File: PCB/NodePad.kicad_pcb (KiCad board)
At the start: 4 copper layers, 100 x 100 mm, 0 parts

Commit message: auto-commit for 1e42cf4f-3af1-430f-b4bd-a55f7dad9cb4
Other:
- board text added: "CERN-OHL-P v2 - Made with love"
- board text added: "Samrath Sami Singh"
- board text added: "by Samrath Sami Singh"
- board text added: "github.com/Sami9889/NodePad"
- board text removed: "Sami9889 - CERN-OHL-P v2"
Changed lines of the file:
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@@
 	(gr_text "NodePad" (at 50 20 0) (layer "F.SilkS")
 		(effects (font (size 3 3) (thickness 0.5) (bold yes)) (justify bottom)))
-	(gr_text "Radxa CM5 carrier - rev 0.1" (at 50 25 0) (layer "F.SilkS")
-		(effects (font (size 1.2 1.2) (thickness 0.2)) (justify bottom)))
-	(gr_text "Sami9889 - CERN-OHL-P v2" (at 50 92 0) (layer "F.SilkS")
+	(gr_text "by Samrath Sami Singh" (at 50 24 0) (layer "F.SilkS")
+		(effects (font (size 1.5 1.5) (thickness 0.25) (italic yes)) (justify bottom)))
+	(gr_text "Radxa CM5 carrier - rev 0.1" (at 50 28 0) (layer "F.SilkS")
+		(effects (font (size 1 1) (thickness 0.15)) (justify bottom)))
+	(gr_text "github.com/Sami9889/NodePad" (at 50 92 0) (layer "F.SilkS")
 		(effects (font (size 1 1) (thickness 0.15)) (justify top)))
+	(gr_text "Samrath Sami Singh" (at 50 8 0) (layer "B.SilkS")
+		(effects (font (size 2 2) (thickness 0.3) (bold yes)) (justify bottom mirror)))
+	(gr_text "CERN-OHL-P v2  -  Made with love" (at 50 12 0) (layer "B.SilkS")
+		(effects (font (size 1 1) (thickness 0.15) (italic yes)) (justify bottom mirror)))
 	(gr_text "CM5 SoM zone" (at 50 55 0) (layer "F.Fab")
 		(effects (font (size 2 2) (thickness 0.3))))

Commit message: Auto-generated changes
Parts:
- added BT1: CR2032, BatteryHolder_Keystone_3002_1x2032, F.Cu at (10.0, 45.0)
- added C1: 1uF, C_0402_1005Metric, F.Cu at (15.5, 45.0)
- added C10: 22uF/25V, C_0805_2012Metric, F.Cu at (21.0, 45.0)
- added C11: 22uF/25V, C_0805_2012Metric, F.Cu at (26.5, 45.0)
- added C12: 10uF/16V, C_0402_1005Metric, F.Cu at (32.0, 45.0)
- added C13: 100nF, C_0402_1005Metric, F.Cu at (37.5, 45.0)
- added C15: 1uF, C_0402_1005Metric, F.Cu at (43.0, 45.0)
- added C16: 1uF, C_0402_1005Metric, F.Cu at (48.5, 45.0)
- added C2: 1uF, C_0402_1005Metric, F.Cu at (54.0, 45.0)
- added C3: 22uF/25V, C_0805_2012Metric, F.Cu at (59.5, 45.0)
- added C4: 100nF, C_0402_1005Metric, F.Cu at (65.0, 45.0)
- added C5: 2.2nF, C_0402_1005Metric, F.Cu at (70.5, 45.0)
- added C6: 100pF, C_0402_1005Metric, F.Cu at (76.0, 45.0)
- added C_AVDD_BULK_1: 10uF, C_0805_2012Metric, F.Cu at (81.5, 45.0)
- added C_AVDD_BULK_2: 10uF, C_0805_2012Metric, F.Cu at (87.0, 45.0)
- added C_AVDD_BULK_3: 10uF, C_0805_2012Metric, F.Cu at (92.5, 45.0)
- added C_AVDD_BULK_4: 10uF, C_0805_2012Metric, F.Cu at (10.0, 50.5)
- added C_AVDD_HF_1: 100nF, C_0402_1005Metric, F.Cu at (15.5, 50.5)
- added C_AVDD_HF_2: 100nF, C_0402_1005Metric, F.Cu at (21.0, 50.5)
- added C_AVDD_HF_3: 100nF, C_0402_1005Metric, F.Cu at (26.5, 50.5)
- added C_AVDD_HF_4: 100nF, C_0402_1005Metric, F.Cu at (32.0, 50.5)
- added C_BAT_1: 100nF, C_0402_1005Metric, F.Cu at (37.5, 50.5)
- added C_BLK_3V3_AUX_01: 10uF, C_0805_2012Metric, F.Cu at (43.0, 50.5)
- added C_BLK_3V3_AUX_02: 10uF, C_0805_2012Metric, F.Cu at (48.5, 50.5)
- added C_BLK_3V3_AUX_03: 10uF, C_0805_2012Metric, F.Cu at (54.0, 50.5)
- added C_BLK_5V_01: 10uF, C_0805_2012Metric, F.Cu at (59.5, 50.5)
- added C_BLK_5V_02: 10uF, C_0805_2012Metric, F.Cu at (65.0, 50.5)
- added C_BLK_5V_03: 10uF, C_0805_2012Metric, F.Cu at (70.5, 50.5)
- added C_BLK_5V_04: 10uF, C_0805_2012Metric, F.Cu at (76.0, 50.5)
- added C_BS_J3: 1nF/2kV, C_1210_3225Metric, F.Cu at (81.5, 50.5)
- added C_BS_J4: 1nF/2kV, C_1210_3225Metric, F.Cu at (87.0, 50.5)
- added C_CM5_BULK_1: 10uF, C_0603_1608Metric, F.Cu at (92.5, 50.5)
- added C_CM5_BULK_2: 10uF, C_0603_1608Metric, F.Cu at (10.0, 56.0)
- added C_CM5_BULK_3: 10uF, C_0603_1608Metric, F.Cu at (15.5, 56.0)
- added C_CM5_BULK_4: 10uF, C_0603_1608Metric, F.Cu at (21.0, 56.0)
- added C_CM5_BULK_5: 10uF, C_0603_1608Metric, F.Cu at (26.5, 56.0)
- added C_CM5_BULK_6: 10uF, C_0603_1608Metric, F.Cu at (32.0, 56.0)
- added C_CM5_HF_1: 100nF, C_0402_1005Metric, F.Cu at (37.5, 56.0)
- added C_CM5_HF_10: 100nF, C_0402_1005Metric, F.Cu at (43.0, 56.0)
- added C_CM5_HF_2: 100nF, C_0402_1005Metric, F.Cu at (48.5, 56.0)
- added C_CM5_HF_3: 100nF, C_0402_1005Metric, F.Cu at (54.0, 56.0)
- added C_CM5_HF_4: 100nF, C_0402_1005Metric, F.Cu at (59.5, 56.0)
- added C_CM5_HF_5: 100nF, C_0402_1005Metric, F.Cu at (65.0, 56.0)
- added C_CM5_HF_6: 100nF, C_0402_1005Metric, F.Cu at (70.5, 56.0)
- added C_CM5_HF_7: 100nF, C_0402_1005Metric, F.Cu at (76.0, 56.0)
- added C_CM5_HF_8: 100nF, C_0402_1005Metric, F.Cu at (81.5, 56.0)
- added C_CM5_HF_9: 100nF, C_0402_1005Metric, F.Cu at (87.0, 56.0)
- added C_DEC_3V3_AUX_01: 100nF, C_0402_1005Metric, F.Cu at (92.5, 56.0)
- added C_DEC_3V3_AUX_02: 100nF, C_0402_1005Metric, F.Cu at (10.0, 61.5)
- added C_DEC_3V3_AUX_03: 100nF, C_0402_1005Metric, F.Cu at (15.5, 61.5)
- added C_DEC_3V3_AUX_04: 100nF, C_0402_1005Metric, F.Cu at (21.0, 61.5)
- added C_DEC_3V3_AUX_05: 100nF, C_0402_1005Metric, F.Cu at (26.5, 61.5)
- added C_DEC_3V3_AUX_06: 100nF, C_0402_1005Metric, F.Cu at (32.0, 61.5)
- added C_DEC_3V3_AUX_07: 100nF, C_0402_1005Metric, F.Cu at (37.5, 61.5)
- added C_DEC_3V3_AUX_08: 100nF, C_0402_1005Metric, F.Cu at (43.0, 61.5)
- added C_DEC_3V3_AUX_09: 100nF, C_0402_1005Metric, F.Cu at (48.5, 61.5)
- added C_DEC_3V3_AUX_10: 100nF, C_0402_1005Metric, F.Cu at (54.0, 61.5)
- added C_DEC_5V_01: 100nF, C_0402_1005Metric, F.Cu at (59.5, 61.5)
- added C_DEC_5V_02: 100nF, C_0402_1005Metric, F.Cu at (65.0, 61.5)
- added C_DEC_5V_03: 100nF, C_0402_1005Metric, F.Cu at (70.5, 61.5)
- added C_DEC_5V_04: 100nF, C_0402_1005Metric, F.Cu at (76.0, 61.5)
- added C_DEC_5V_05: 100nF, C_0402_1005Metric, F.Cu at (81.5, 61.5)
- added C_DEC_5V_06: 100nF, C_0402_1005Metric, F.Cu at (87.0, 61.5)
- added C_DEC_5V_07: 100nF, C_0402_1005Metric, F.Cu at (92.5, 61.5)
- added C_DEC_5V_08: 100nF, C_0402_1005Metric, F.Cu at (10.0, 67.0)
- added C_DEC_5V_09: 100nF, C_0402_1005Metric, F.Cu at (15.5, 67.0)
- added C_DEC_5V_10: 100nF, C_0402_1005Metric, F.Cu at (21.0, 67.0)
- added C_DEC_5V_11: 100nF, C_0402_1005Metric, F.Cu at (26.5, 67.0)
- added C_DEC_5V_12: 100nF, C_0402_1005Metric, F.Cu at (32.0, 67.0)
- added C_EMI: 1nF/2kV, C_1210_3225Metric, F.Cu at (37.5, 67.0)
- added C_HUB_1: 100nF, C_0402_1005Metric, F.Cu at (43.0, 67.0)
- added C_HUB_2: 100nF, C_0402_1005Metric, F.Cu at (48.5, 67.0)
- added C_HUB_3: 100nF, C_0402_1005Metric, F.Cu at (54.0, 67.0)
- added C_HUB_4: 100nF, C_0402_1005Metric, F.Cu at (59.5, 67.0)
- added C_HUB_5: 100nF, C_0402_1005Metric, F.Cu at (65.0, 67.0)
- added C_HUB_6: 100nF, C_0402_1005Metric, F.Cu at (70.5, 67.0)
- added C_HUB_7: 100nF, C_0402_1005Metric, F.Cu at (76.0, 67.0)
- added C_HUB_8: 100nF, C_0402_1005Metric, F.Cu at (81.5, 67.0)
- added C_HUB_BULK: 10uF, C_0603_1608Metric, F.Cu at (87.0, 67.0)
- added C_HUB_LDO: 4.7uF, C_0603_1608Metric, F.Cu at (92.5, 67.0)
- added C_M2E_1: 100nF, C_0402_1005Metric, F.Cu at (10.0, 72.5)
- added C_M2E_2: 100nF, C_0402_1005Metric, F.Cu at (15.5, 72.5)
- added C_M2E_3: 100nF, C_0402_1005Metric, F.Cu at (21.0, 72.5)
- added C_M2E_BULK: 10uF, C_0603_1608Metric, F.Cu at (26.5, 72.5)
- added C_M2M_1: 100nF, C_0402_1005Metric, F.Cu at (32.0, 72.5)
- added C_M2M_2: 100nF, C_0402_1005Metric, F.Cu at (37.5, 72.5)
- added C_M2M_3: 100nF, C_0402_1005Metric, F.Cu at (43.0, 72.5)
- added C_M2M_4: 100nF, C_0402_1005Metric, F.Cu at (48.5, 72.5)
- added C_M2M_BULK: 22uF/6.3V, C_0805_2012Metric, F.Cu at (54.0, 72.5)
- added C_POE_BULK: 22uF/100V DNP, C_1210_3225Metric, F.Cu at (59.5, 72.5)
- added C_POE_HF: 100nF/100V DNP, C_1206_3216Metric, F.Cu at (65.0, 72.5)
- added C_POE_SEC: 47uF/25V DNP, C_1210_3225Metric, F.Cu at (70.5, 72.5)
- added C_PWR_EN_DLY: 470nF, C_0402_1005Metric, F.Cu at (76.0, 72.5)
- added C_RESET_DB: 100nF, C_0402_1005Metric, F.Cu at (81.5, 72.5)
- added C_RTC_1: 100nF, C_0402_1005Metric, F.Cu at (87.0, 72.5)
- added C_RTC_2: 1uF, C_0402_1005Metric, F.Cu at (92.5, 72.5)
- added C_RTL_1: 100nF, C_0402_1005Metric, F.Cu at (10.0, 78.0)
- added C_RTL_2: 100nF, C_0402_1005Metric, F.Cu at (15.5, 78.0)
- added C_RTL_3: 100nF, C_0402_1005Metric, F.Cu at (21.0, 78.0)
- added C_RTL_4: 100nF, C_0402_1005Metric, F.Cu at (26.5, 78.0)
- added C_RTL_5: 100nF, C_0402_1005Metric, F.Cu at (32.0, 78.0)
- added C_RTL_6: 100nF, C_0402_1005Metric, F.Cu at (37.5, 78.0)
- added C_RTL_BULK: 10uF, C_0603_1608Metric, F.Cu at (43.0, 78.0)
- added C_VB_J10: 150uF/6.3V, C_1206_3216Metric, F.Cu at (48.5, 78.0)
- added C_VB_J11: 150uF/6.3V, C_1206_3216Metric, F.Cu at (54.0, 78.0)
- added C_VB_J8: 150uF/6.3V, C_1206_3216Metric, F.Cu at (59.5, 78.0)
- added C_VB_J9: 150uF/6.3V, C_1206_3216Metric, F.Cu at (65.0, 78.0)
- added C_VIN_BULK: 47uF/25V, CP_Elec_5x5.4, F.Cu at (70.5, 78.0)
- added C_VIN_HF: 100nF, C_0402_1005Metric, F.Cu at (76.0, 78.0)
- added D1: Green, LED_0603_1608Metric, F.Cu at (81.5, 78.0)
- added D2: Blue, LED_0603_1608Metric, F.Cu at (87.0, 78.0)
- added D3: Yellow, LED_0603_1608Metric, F.Cu at (92.5, 78.0)
- added D4: Yellow, LED_0603_1608Metric, F.Cu at (10.0, 83.5)
- added D5: Red, LED_0603_1608Metric, F.Cu at (15.5, 83.5)
- added D6: SMBJ12A, D_SMB, F.Cu at (21.0, 83.5)
- added D_BAT: BAT54, D_SOD-323, F.Cu at (26.5, 83.5)
- added D_HDMI_CTL_1: ESD5Z5.0, D_SOD-523, F.Cu at (32.0, 83.5)
- added D_HDMI_CTL_2: ESD5Z5.0, D_SOD-523, F.Cu at (37.5, 83.5)
- added D_POE_1: HD01-T DNP, D_SMB, F.Cu at (43.0, 83.5)
- added D_POE_2: HD01-T DNP, D_SMB, F.Cu at (48.5, 83.5)
- added D_POE_3: HD01-T DNP, D_SMB, F.Cu at (54.0, 83.5)
- added D_POE_4: HD01-T DNP, D_SMB, F.Cu at (59.5, 83.5)
- added D_POE_OR: SS36 DNP, D_SMB, F.Cu at (65.0, 83.5)
- added D_POE_SEC: SS36 DNP, D_SMB, F.Cu at (70.5, 83.5)
- added D_POE_TVS: SMBJ58A DNP, D_SMB, F.Cu at (76.0, 83.5)
- added D_TVS_J10: SMBJ5.0A, D_SMB, F.Cu at (81.5, 83.5)
- added D_TVS_J11: SMBJ5.0A, D_SMB, F.Cu at (87.0, 83.5)
- added D_TVS_J8: SMBJ5.0A, D_SMB, F.Cu at (92.5, 83.5)
- added D_TVS_J9: SMBJ5.0A, D_SMB, F.Cu at (10.0, 89.0)
- added FB_AVDD_1: 600R@100MHz, L_0603_1608Metric, F.Cu at (15.5, 89.0)
- added FB_AVDD_2: 600R@100MHz, L_0603_1608Metric, F.Cu at (21.0, 89.0)
- added FB_AVDD_3: 600R@100MHz, L_0603_1608Metric, F.Cu at (26.5, 89.0)
- added FB_AVDD_4: 600R@100MHz, L_0603_1608Metric, F.Cu at (32.0, 89.0)
- added FB_HDMI_5V: 600R@100MHz, L_0603_1608Metric, F.Cu at (37.5, 89.0)
- added J1: CM5-J1, Hirose_BM24_BM24-40DS-2-0.35V_2x20_P0.35mm_PowerPin2_Vertical, F.Cu at (43.0, 89.0)
- added J10: USB3-A, USB3_A_Molex_48393-001, F.Cu at (48.5, 89.0)
- added J11: USB3-A, USB3_A_Molex_48393-001, F.Cu at (54.0, 89.0)
- added J12: HDMI, HDMI_A_Molex_208658-1001_Horizontal, F.Cu at (59.5, 89.0)
- added J13: GPIO40, PinHeader_2x20_P2.54mm_Vertical, F.Cu at (65.0, 89.0)
- added J15: Fan, PinHeader_1x04_P2.54mm_Vertical, F.Cu at (70.5, 89.0)
- added J2: CM5-J2, Hirose_BM24_BM24-40DS-2-0.35V_2x20_P0.35mm_PowerPin2_Vertical, F.Cu at (76.0, 89.0)
- added J3: RJ45, RJ45_Amphenol_RJHSE538X-02, F.Cu at (81.5, 89.0)
- added J4: RJ45, RJ45_Amphenol_RJHSE538X-02, F.Cu at (87.0, 89.0)
- added J5: M.2 M-key 2280, PinHeader_2x38_P1.27mm_Vertical_SMD, F.Cu at (92.5, 89.0)
- added J6: M.2 E-key 2230, PinHeader_2x38_P1.27mm_Vertical_SMD, F.Cu at (10.0, 94.5)
- added J7: USB-C, USB_C_Receptacle_HRO_TYPE-C-31-M-12, F.Cu at (15.5, 94.5)
- added J8: USB3-A, USB3_A_Molex_48393-001, F.Cu at (21.0, 94.5)
- added J9: USB3-A, USB3_A_Molex_48393-001, F.Cu at (26.5, 94.5)
- added L1: 4.7uH/3A, L_Bourns_SRR1208_12.7x12.7mm, F.Cu at (32.0, 94.5)
- added MH1: M2.5 heatsink, MountingHole_2.7mm_M2.5, F.Cu at (37.5, 94.5)
- added MH2: M2.5 heatsink, MountingHole_2.7mm_M2.5, F.Cu at (43.0, 94.5)
- added MH3: M2.5 heatsink, MountingHole_2.7mm_M2.5, F.Cu at (48.5, 94.5)
- added MH4: M2.5 heatsink, MountingHole_2.7mm_M2.5, F.Cu at (54.0, 94.5)
- added Q_DDC_1: BSS138, SOT-23, F.Cu at (59.5, 94.5)
- added Q_DDC_2: BSS138, SOT-23, F.Cu at (65.0, 94.5)
- added R1: 10k, R_0402_1005Metric, F.Cu at (70.5, 94.5)
- added R2: 10k, R_0402_1005Metric, F.Cu at (76.0, 94.5)
- added R3: 0, R_0402_1005Metric, F.Cu at (81.5, 94.5)
- added R4: 100k, R_0402_1005Metric, F.Cu at (87.0, 94.5)
- added R5: 52.3k, R_0402_1005Metric, F.Cu at (92.5, 94.5)
- added R6: 10k, R_0402_1005Metric, F.Cu at (10.0, 100.0)
- added R7: 10k, R_0402_1005Metric, F.Cu at (15.5, 100.0)
- added R_BOOT0_PU: 10k, R_0402_1005Metric, F.Cu at (21.0, 100.0)
- added R_BOOT1_PU: 10k, R_0402_1005Metric, F.Cu at (26.5, 100.0)
- added R_BOOT2_PU: 10k, R_0402_1005Metric, F.Cu at (32.0, 100.0)
- added R_BS_J3_1: 75, R_0402_1005Metric, F.Cu at (37.5, 100.0)
- added R_BS_J3_2: 75, R_0402_1005Metric, F.Cu at (43.0, 100.0)
- added R_BS_J3_3: 75, R_0402_1005Metric, F.Cu at (48.5, 100.0)
- added R_BS_J3_4: 75, R_0402_1005Metric, F.Cu at (54.0, 100.0)
- added R_BS_J3_5: 75, R_0402_1005Metric, F.Cu at (59.5, 100.0)
- added R_BS_J3_6: 75, R_0402_1005Metric, F.Cu at (65.0, 100.0)
- added R_BS_J3_7: 75, R_0402_1005Metric, F.Cu at (70.5, 100.0)
- added R_BS_J3_8: 75, R_0402_1005Metric, F.Cu at (76.0, 100.0)
- added R_BS_J4_1: 75, R_0402_1005Metric, F.Cu at (81.5, 100.0)
- added R_BS_J4_2: 75, R_0402_1005Metric, F.Cu at (87.0, 100.0)
- added R_BS_J4_3: 75, R_0402_1005Metric, F.Cu at (92.5, 100.0)
- added R_BS_J4_4: 75, R_0402_1005Metric, F.Cu at (10.0, 105.5)
- added R_BS_J4_5: 75, R_0402_1005Metric, F.Cu at (15.5, 105.5)
- added R_BS_J4_6: 75, R_0402_1005Metric, F.Cu at (21.0, 105.5)
- added R_BS_J4_7: 75, R_0402_1005Metric, F.Cu at (26.5, 105.5)
- added R_BS_J4_8: 75, R_0402_1005Metric, F.Cu at (32.0, 105.5)
- added R_D1: 1k, R_0402_1005Metric, F.Cu at (37.5, 105.5)
- added R_D2: 1k, R_0402_1005Metric, F.Cu at (43.0, 105.5)
- added R_D3: 1k, R_0402_1005Metric, F.Cu at (48.5, 105.5)
- added R_D4: 1k, R_0402_1005Metric, F.Cu at (54.0, 105.5)
- added R_D5: 1k, R_0402_1005Metric, F.Cu at (59.5, 105.5)
- added R_DDC_G_1: 10k, R_0402_1005Metric, F.Cu at (65.0, 105.5)
- added R_DDC_G_2: 10k, R_0402_1005Metric, F.Cu at (70.5, 105.5)
- added R_DDC_HI_1: 10k, R_0402_1005Metric, F.Cu at (76.0, 105.5)
- added R_DDC_HI_2: 10k, R_0402_1005Metric, F.Cu at (81.5, 105.5)
- added R_DDC_LO_1: 10k, R_0402_1005Metric, F.Cu at (87.0, 105.5)
- added R_DDC_LO_2: 10k, R_0402_1005Metric, F.Cu at (92.5, 105.5)
- added R_DDC_SCL: 2.2k, R_0402_1005Metric, F.Cu at (10.0, 111.0)
- added R_DDC_SCL_SER: 100, R_0402_1005Metric, F.Cu at (15.5, 111.0)
- added R_DDC_SDA: 2.2k, R_0402_1005Metric, F.Cu at (21.0, 111.0)
- added R_DDC_SDA_SER: 100, R_0402_1005Metric, F.Cu at (26.5, 111.0)
- added R_E_OPT_1: 0/DNP, R_0402_1005Metric, F.Cu at (32.0, 111.0)
- added R_E_OPT_2: 0/DNP, R_0402_1005Metric, F.Cu at (37.5, 111.0)
- added R_E_OPT_3: 0/DNP, R_0402_1005Metric, F.Cu at (43.0, 111.0)
- added R_E_OPT_4: 0/DNP, R_0402_1005Metric, F.Cu at (48.5, 111.0)
- added R_HUB_BP: 10k, R_0402_1005Metric, F.Cu at (54.0, 111.0)
- added R_HUB_RST: 10k, R_0402_1005Metric, F.Cu at (59.5, 111.0)
- added R_I2C1_SCL_PU: 4.7k, R_0402_1005Metric, F.Cu at (65.0, 111.0)
- added R_I2C1_SDA_PU: 4.7k, R_0402_1005Metric, F.Cu at (70.5, 111.0)
- added R_ILIM_J10: 30k, R_0402_1005Metric, F.Cu at (76.0, 111.0)
- added R_ILIM_J11: 30k, R_0402_1005Metric, F.Cu at (81.5, 111.0)
- added R_ILIM_J8: 30k, R_0402_1005Metric, F.Cu at (87.0, 111.0)
- added R_ILIM_J9: 30k, R_0402_1005Metric, F.Cu at (92.5, 111.0)
- added R_INT_PU: 10k, R_0402_1005Metric, F.Cu at (10.0, 116.5)
- added R_M2M_PERST: 10k, R_0402_1005Metric, F.Cu at (15.5, 116.5)
- added R_MASKROM_PU: 10k, R_0402_1005Metric, F.Cu at (21.0, 116.5)
- added R_NVME_ACT_PU: 10k, R_0402_1005Metric, F.Cu at (26.5, 116.5)
- added R_PCIE0_TERM_N: 49.9 DNP, R_0402_1005Metric, F.Cu at (32.0, 116.5)
- added R_PCIE0_TERM_P: 49.9 DNP, R_0402_1005Metric, F.Cu at (37.5, 116.5)
- added R_POE_CLASS: 12.5 DNP, R_0402_1005Metric, F.Cu at (43.0, 116.5)
- added R_POE_SIG: 25k DNP, R_0402_1005Metric, F.Cu at (48.5, 116.5)
- added R_PU_PCIE0_CLKREQ: 10k, R_0402_1005Metric, F.Cu at (54.0, 116.5)
- added R_PU_PCIE0_PERST: 10k, R_0402_1005Metric, F.Cu at (59.5, 116.5)
- added R_PU_PCIE1_CLKREQ: 10k, R_0402_1005Metric, F.Cu at (65.0, 116.5)
- added R_PU_PCIE1_PERST: 10k, R_0402_1005Metric, F.Cu at (70.5, 116.5)
- added R_PWR_EN_DLY: 100k, R_0402_1005Metric, F.Cu at (76.0, 116.5)
- added R_RESET_PU: 10k, R_0402_1005Metric, F.Cu at (81.5, 116.5)
- added R_SCL_PU: 4.7k, R_0402_1005Metric, F.Cu at (87.0, 116.5)
- added R_SDA_PU: 4.7k, R_0402_1005Metric, F.Cu at (92.5, 116.5)
- added SW1: RESET, SW_SPST_TL3305A, F.Cu at (10.0, 122.0)
- added SW2: BOOT, SW_SPST_TL3305A, F.Cu at (15.5, 122.0)
- added T1: 750317847 DNP, DIP-8_W7.62mm, F.Cu at (21.0, 122.0)
- added TP1: TP, TestPoint_Pad_D1.5mm, F.Cu at (26.5, 122.0)
- added TP2: TP, TestPoint_Pad_D1.5mm, F.Cu at (32.0, 122.0)
- added TP3: TP, TestPoint_Pad_D1.5mm, F.Cu at (37.5, 122.0)
- added TP4: TP, TestPoint_Pad_D1.5mm, F.Cu at (43.0, 122.0)
- added TP5: TP, TestPoint_Pad_D1.5mm, F.Cu at (48.5, 122.0)
- added U10: GL3523, ArtInChip_QFN-88-1EP_10x10mm_P0.4mm_EP6.74x6.74mm, F.Cu at (54.0, 122.0)
- added U11: TPS2553, SOT-23-6, F.Cu at (59.5, 122.0)
- added U12: TPS2553, SOT-23-6, F.Cu at (65.0, 122.0)
- added U13: TPS2553, SOT-23-6, F.Cu at (70.5, 122.0)
- added U14: TPS2553, SOT-23-6, F.Cu at (76.0, 122.0)
- added U2: RTL8125BG, QFN-64-1EP_9x9mm_P0.5mm_EP4.7x4.7mm, F.Cu at (81.5, 122.0)
- added U3: MP2315, SOT-563, F.Cu at (87.0, 122.0)
- added U4: AP2112K-3.3, SOT-23-5, F.Cu at (92.5, 122.0)
- added U5: CH224K, VSSOP-10_3x3mm_P0.5mm, F.Cu at (10.0, 127.5)
- added U6: MP8007 DNP, SOIC-16_3.9x9.9mm_P1.27mm, F.Cu at (15.5, 127.5)
- added U7: DS3231MZ+, SOIC-8_3.9x4.9mm_P1.27mm, F.Cu at (21.0, 127.5)
- added U_HDMI_ESD_1: USBLC6-2SC6, SOT-23-6, F.Cu at (26.5, 127.5)
- added U_HDMI_ESD_2: USBLC6-2SC6, SOT-23-6, F.Cu at (32.0, 127.5)
- added U_HDMI_ESD_3: USBLC6-2SC6, SOT-23-6, F.Cu at (37.5, 127.5)
- added U_HDMI_ESD_4: USBLC6-2SC6, SOT-23-6, F.Cu at (43.0, 127.5)
- added Y1: 25MHz TCXO, Crystal_SMD_3225-4Pin_3.2x2.5mm, F.Cu at (48.5, 127.5)
- added Y_HUB: 25MHz, Crystal_SMD_3225-4Pin_3.2x2.5mm, F.Cu at (54.0, 127.5)

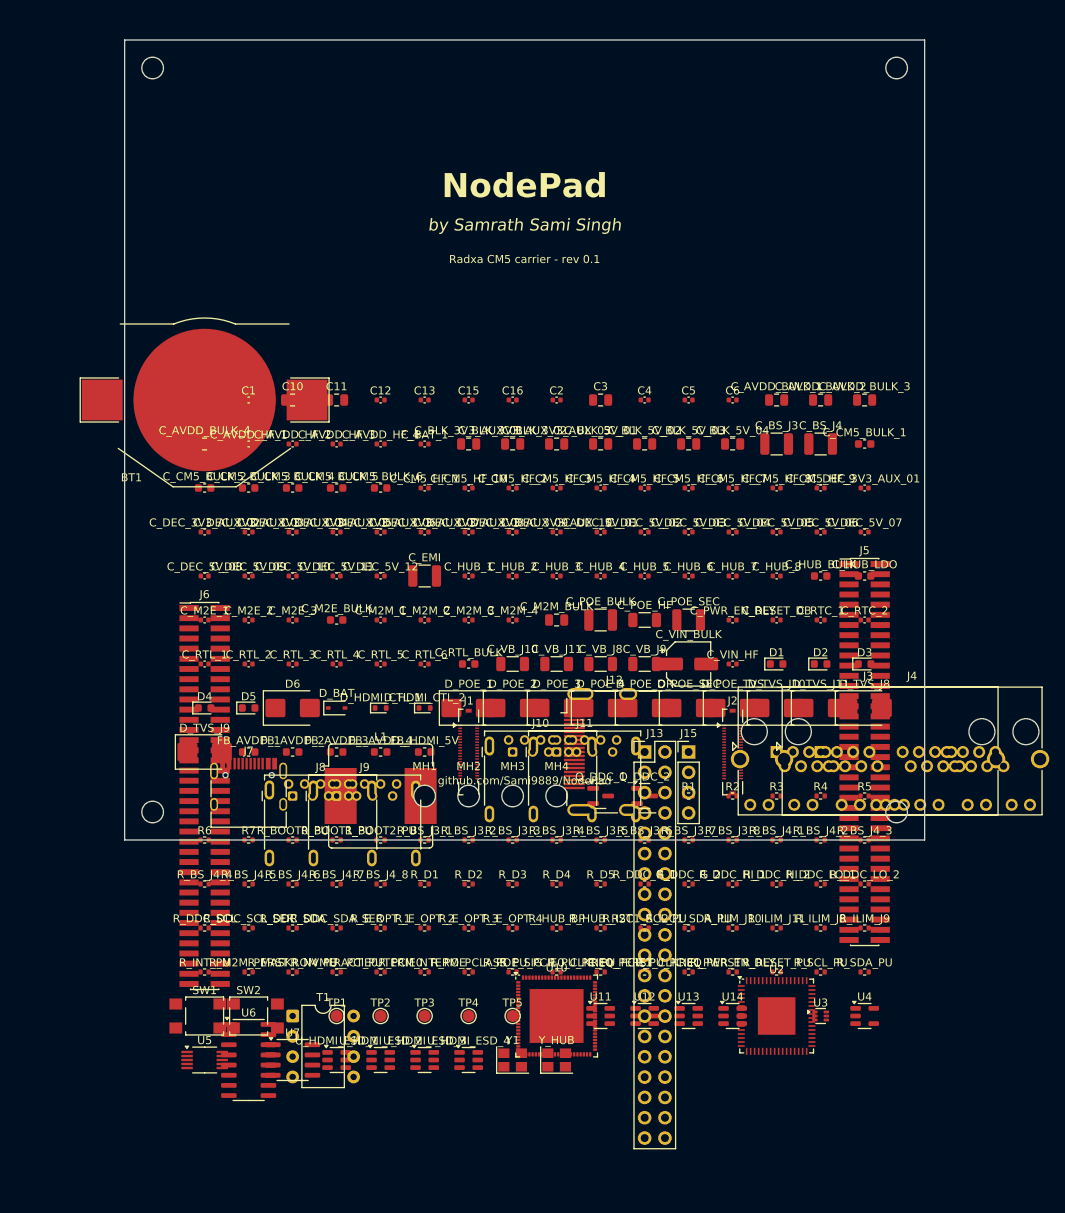
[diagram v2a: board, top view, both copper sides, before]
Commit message: refactor: relocate components and add net assignments on PCB/NodePad.kicad_pcb
Co-authored-by: Sami.s <191058343+Sami9889@users.noreply.github.com>
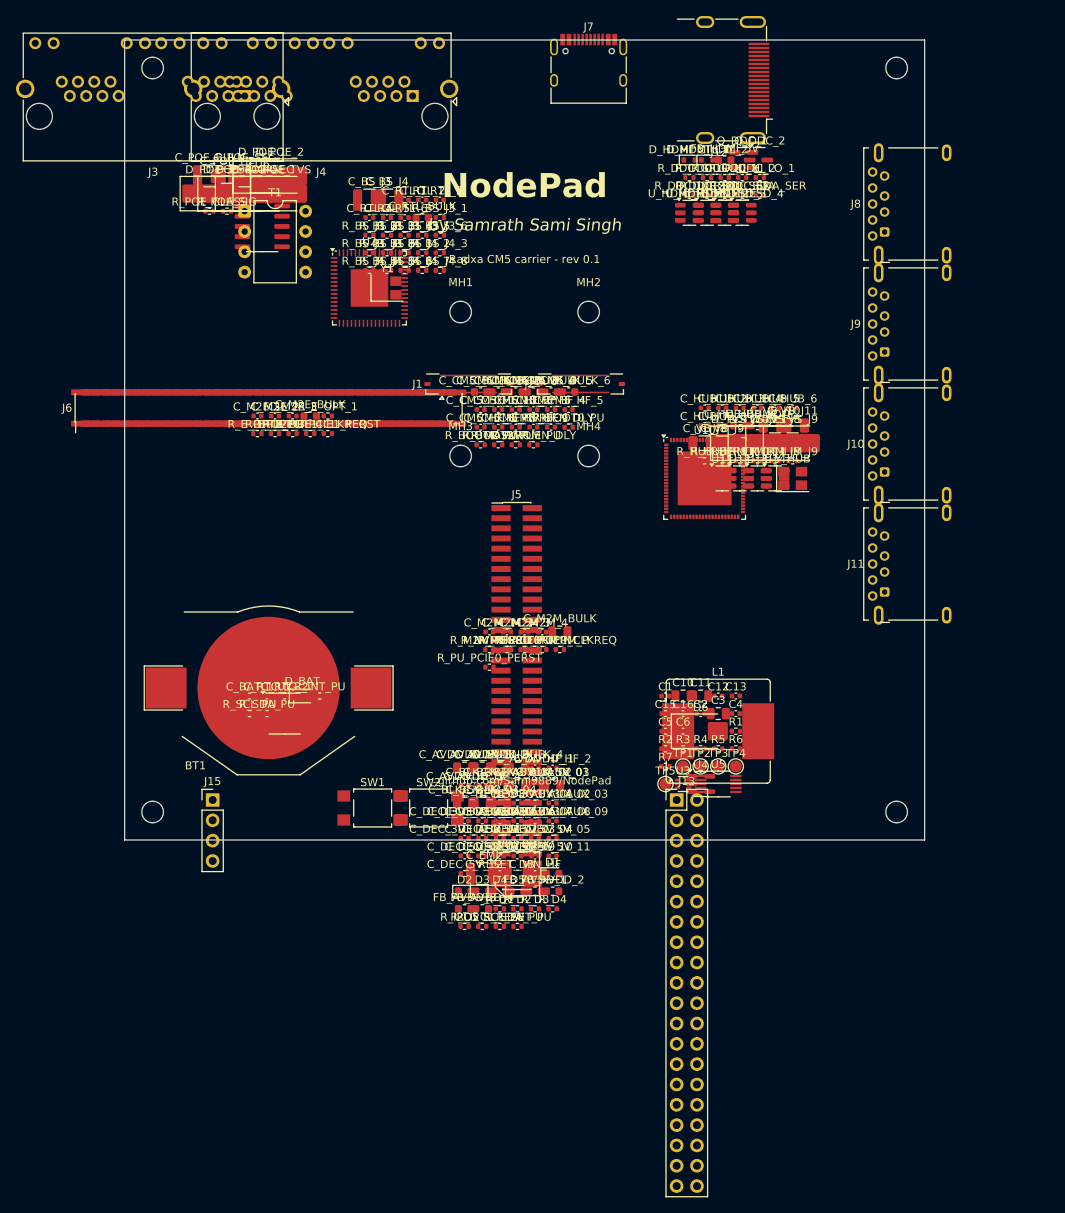
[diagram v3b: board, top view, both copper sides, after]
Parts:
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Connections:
- BT1 pad 1: (no net) -> N$21
- BT1 pad 2: (no net) -> GND
- C1 pad 1: (no net) -> VBUS_USB1
- C1 pad 2: (no net) -> GND1
- C10 pad 1: (no net) -> +5V1
- C10 pad 2: (no net) -> GND1
- C11 pad 1: (no net) -> +5V1
- C11 pad 2: (no net) -> GND1
- C12 pad 1: (no net) -> +5V1
- C12 pad 2: (no net) -> GND1
- C13 pad 1: (no net) -> +5V1
- C13 pad 2: (no net) -> GND1
- C15 pad 1: (no net) -> +5V1
- C15 pad 2: (no net) -> GND1
- C16 pad 1: (no net) -> +3V3_AUX1
- C16 pad 2: (no net) -> GND1
- C2 pad 1: (no net) -> VIN_12V1
- C2 pad 2: (no net) -> GND1
- C3 pad 1: (no net) -> VIN_12V1
- C3 pad 2: (no net) -> GND1
- C4 pad 1: (no net) -> N$6
- C4 pad 2: (no net) -> SW_5V
- C5 pad 1: (no net) -> N$9
- C5 pad 2: (no net) -> GND1
- C6 pad 1: (no net) -> N$8
- C6 pad 2: (no net) -> GND1
- C_AVDD_BULK_1 pad 1: (no net) -> AVDD_HDMI2
- C_AVDD_BULK_1 pad 2: (no net) -> GND
- C_AVDD_BULK_2 pad 1: (no net) -> AVDD_PCIE2
- C_AVDD_BULK_2 pad 2: (no net) -> GND
- C_AVDD_BULK_3 pad 1: (no net) -> AVDD_ETH0_2
- C_AVDD_BULK_3 pad 2: (no net) -> GND
- C_AVDD_BULK_4 pad 1: (no net) -> AVDD_ETH1_2
- C_AVDD_BULK_4 pad 2: (no net) -> GND
- C_AVDD_HF_1 pad 1: (no net) -> AVDD_HDMI1
- C_AVDD_HF_1 pad 2: (no net) -> GND
- C_AVDD_HF_2 pad 1: (no net) -> AVDD_PCIE1
- C_AVDD_HF_2 pad 2: (no net) -> GND
- C_AVDD_HF_3 pad 1: (no net) -> AVDD_ETH0_1
- C_AVDD_HF_3 pad 2: (no net) -> GND
- C_AVDD_HF_4 pad 1: (no net) -> AVDD_ETH1_1
- C_AVDD_HF_4 pad 2: (no net) -> GND
- C_BAT_1 pad 1: (no net) -> V_BAT
- C_BAT_1 pad 2: (no net) -> GND
- C_BLK_3V3_AUX_01 pad 1: (no net) -> +3V3_AUX
- C_BLK_3V3_AUX_01 pad 2: (no net) -> GND
- C_BLK_3V3_AUX_02 pad 1: (no net) -> +3V3_AUX
- C_BLK_3V3_AUX_02 pad 2: (no net) -> GND
- C_BLK_3V3_AUX_03 pad 1: (no net) -> +3V3_AUX
- C_BLK_3V3_AUX_03 pad 2: (no net) -> GND
- C_BLK_5V_01 pad 1: (no net) -> +5V
- C_BLK_5V_01 pad 2: (no net) -> GND
- C_BLK_5V_02 pad 1: (no net) -> +5V
- C_BLK_5V_02 pad 2: (no net) -> GND
- C_BLK_5V_03 pad 1: (no net) -> +5V
- C_BLK_5V_03 pad 2: (no net) -> GND
- C_BLK_5V_04 pad 1: (no net) -> +5V
- C_BLK_5V_04 pad 2: (no net) -> GND
- C_BS_J3 pad 1: (no net) -> BOBSMITH_J3
- C_BS_J3 pad 2: (no net) -> CHASSIS_GND
- C_BS_J4 pad 1: (no net) -> BOBSMITH_J4
- C_BS_J4 pad 2: (no net) -> CHASSIS_GND
- C_CM5_BULK_1 pad 1: (no net) -> +5V
- C_CM5_BULK_1 pad 2: (no net) -> GND
- C_CM5_BULK_2 pad 1: (no net) -> +5V
- C_CM5_BULK_2 pad 2: (no net) -> GND
- C_CM5_BULK_3 pad 1: (no net) -> +5V
- C_CM5_BULK_3 pad 2: (no net) -> GND
- C_CM5_BULK_4 pad 1: (no net) -> +5V
- C_CM5_BULK_4 pad 2: (no net) -> GND
- C_CM5_BULK_5 pad 1: (no net) -> +5V
- C_CM5_BULK_5 pad 2: (no net) -> GND
- C_CM5_BULK_6 pad 1: (no net) -> +5V
- C_CM5_BULK_6 pad 2: (no net) -> GND
- C_CM5_HF_1 pad 1: (no net) -> +5V
- C_CM5_HF_1 pad 2: (no net) -> GND
- C_CM5_HF_10 pad 1: (no net) -> +5V
- C_CM5_HF_10 pad 2: (no net) -> GND
- C_CM5_HF_2 pad 1: (no net) -> +5V
- C_CM5_HF_2 pad 2: (no net) -> GND
- C_CM5_HF_3 pad 1: (no net) -> +5V
- C_CM5_HF_3 pad 2: (no net) -> GND
- C_CM5_HF_4 pad 1: (no net) -> +5V
- C_CM5_HF_4 pad 2: (no net) -> GND
- C_CM5_HF_5 pad 1: (no net) -> +5V
- C_CM5_HF_5 pad 2: (no net) -> GND
- C_CM5_HF_6 pad 1: (no net) -> +5V
- C_CM5_HF_6 pad 2: (no net) -> GND
- C_CM5_HF_7 pad 1: (no net) -> +5V
- C_CM5_HF_7 pad 2: (no net) -> GND
- C_CM5_HF_8 pad 1: (no net) -> +5V
- C_CM5_HF_8 pad 2: (no net) -> GND
- C_CM5_HF_9 pad 1: (no net) -> +5V
- C_CM5_HF_9 pad 2: (no net) -> GND
- C_DEC_3V3_AUX_01 pad 1: (no net) -> +3V3_AUX
- C_DEC_3V3_AUX_01 pad 2: (no net) -> GND
- C_DEC_3V3_AUX_02 pad 1: (no net) -> +3V3_AUX
- C_DEC_3V3_AUX_02 pad 2: (no net) -> GND
- C_DEC_3V3_AUX_03 pad 1: (no net) -> +3V3_AUX
- C_DEC_3V3_AUX_03 pad 2: (no net) -> GND
- C_DEC_3V3_AUX_04 pad 1: (no net) -> +3V3_AUX
- C_DEC_3V3_AUX_04 pad 2: (no net) -> GND
- C_DEC_3V3_AUX_05 pad 1: (no net) -> +3V3_AUX
- C_DEC_3V3_AUX_05 pad 2: (no net) -> GND
- C_DEC_3V3_AUX_06 pad 1: (no net) -> +3V3_AUX
- C_DEC_3V3_AUX_06 pad 2: (no net) -> GND
- C_DEC_3V3_AUX_07 pad 1: (no net) -> +3V3_AUX
- C_DEC_3V3_AUX_07 pad 2: (no net) -> GND
- C_DEC_3V3_AUX_08 pad 1: (no net) -> +3V3_AUX
- C_DEC_3V3_AUX_08 pad 2: (no net) -> GND
- C_DEC_3V3_AUX_09 pad 1: (no net) -> +3V3_AUX
- C_DEC_3V3_AUX_09 pad 2: (no net) -> GND
- C_DEC_3V3_AUX_10 pad 1: (no net) -> +3V3_AUX
- C_DEC_3V3_AUX_10 pad 2: (no net) -> GND
- C_DEC_5V_01 pad 1: (no net) -> +5V
- C_DEC_5V_01 pad 2: (no net) -> GND
- C_DEC_5V_02 pad 1: (no net) -> +5V
- C_DEC_5V_02 pad 2: (no net) -> GND
- C_DEC_5V_03 pad 1: (no net) -> +5V
- C_DEC_5V_03 pad 2: (no net) -> GND
- C_DEC_5V_04 pad 1: (no net) -> +5V
- C_DEC_5V_04 pad 2: (no net) -> GND
- C_DEC_5V_05 pad 1: (no net) -> +5V
- C_DEC_5V_05 pad 2: (no net) -> GND
- C_DEC_5V_06 pad 1: (no net) -> +5V
- C_DEC_5V_06 pad 2: (no net) -> GND
- C_DEC_5V_07 pad 1: (no net) -> +5V
- C_DEC_5V_07 pad 2: (no net) -> GND
- C_DEC_5V_08 pad 1: (no net) -> +5V
- C_DEC_5V_08 pad 2: (no net) -> GND
- C_DEC_5V_09 pad 1: (no net) -> +5V
- C_DEC_5V_09 pad 2: (no net) -> GND
- C_DEC_5V_10 pad 1: (no net) -> +5V
- C_DEC_5V_10 pad 2: (no net) -> GND
- C_DEC_5V_11 pad 1: (no net) -> +5V
- C_DEC_5V_11 pad 2: (no net) -> GND
- C_DEC_5V_12 pad 1: (no net) -> +5V
- C_DEC_5V_12 pad 2: (no net) -> GND
- C_EMI pad 1: (no net) -> GND
- C_EMI pad 2: (no net) -> CHASSIS_GND1
- C_HUB_1 pad 1: (no net) -> +3V3_AUX
- C_HUB_1 pad 2: (no net) -> GND
- C_HUB_2 pad 1: (no net) -> +3V3_AUX
- C_HUB_2 pad 2: (no net) -> GND
- C_HUB_3 pad 1: (no net) -> +3V3_AUX
- C_HUB_3 pad 2: (no net) -> GND
- C_HUB_4 pad 1: (no net) -> +3V3_AUX
- C_HUB_4 pad 2: (no net) -> GND
- C_HUB_5 pad 1: (no net) -> +3V3_AUX
- C_HUB_5 pad 2: (no net) -> GND
- C_HUB_6 pad 1: (no net) -> +3V3_AUX
- C_HUB_6 pad 2: (no net) -> GND
- C_HUB_7 pad 1: (no net) -> +3V3_AUX
- C_HUB_7 pad 2: (no net) -> GND
- C_HUB_8 pad 1: (no net) -> +3V3_AUX
- C_HUB_8 pad 2: (no net) -> GND
- C_HUB_BULK pad 1: (no net) -> +3V3_AUX
- C_HUB_BULK pad 2: (no net) -> GND
- C_HUB_LDO pad 1: (no net) -> HUB_VDD11_INT
- C_HUB_LDO pad 2: (no net) -> GND
- C_M2E_1 pad 1: (no net) -> +3V3_AUX
- C_M2E_1 pad 2: (no net) -> GND
- C_M2E_2 pad 1: (no net) -> +3V3_AUX
- C_M2E_2 pad 2: (no net) -> GND
- C_M2E_3 pad 1: (no net) -> +3V3_AUX
- C_M2E_3 pad 2: (no net) -> GND
- C_M2E_BULK pad 1: (no net) -> +3V3_AUX
- C_M2E_BULK pad 2: (no net) -> GND
- C_M2M_1 pad 1: (no net) -> +3V3_AUX
- C_M2M_1 pad 2: (no net) -> GND
- C_M2M_2 pad 1: (no net) -> +3V3_AUX
- C_M2M_2 pad 2: (no net) -> GND
- C_M2M_3 pad 1: (no net) -> +3V3_AUX
- C_M2M_3 pad 2: (no net) -> GND
- C_M2M_4 pad 1: (no net) -> +3V3_AUX
- C_M2M_4 pad 2: (no net) -> GND
- C_M2M_BULK pad 1: (no net) -> +3V3_AUX
- C_M2M_BULK pad 2: (no net) -> GND
- C_POE_BULK pad 1: (no net) -> POE_VIN_POS
- C_POE_BULK pad 2: (no net) -> PoE_GND
- C_POE_HF pad 1: (no net) -> POE_VIN_POS
- C_POE_HF pad 2: (no net) -> PoE_GND
- C_POE_SEC pad 1: (no net) -> PoE_SEC_RECT1
- C_POE_SEC pad 2: (no net) -> GND
- C_PWR_EN_DLY pad 1: (no net) -> CM5_POWER_EN
- C_PWR_EN_DLY pad 2: (no net) -> GND
- C_RESET_DB pad 1: (no net) -> CM5_RUN_N
- C_RESET_DB pad 2: (no net) -> GND
- C_RTC_1 pad 1: (no net) -> +3V3_AUX
- C_RTC_1 pad 2: (no net) -> GND
- C_RTC_2 pad 1: (no net) -> +3V3_AUX
- C_RTC_2 pad 2: (no net) -> GND
- C_RTL_1 pad 1: (no net) -> +3V3_AUX
- C_RTL_1 pad 2: (no net) -> GND
- C_RTL_2 pad 1: (no net) -> +3V3_AUX
- C_RTL_2 pad 2: (no net) -> GND
- C_RTL_3 pad 1: (no net) -> +3V3_AUX
- C_RTL_3 pad 2: (no net) -> GND
- C_RTL_4 pad 1: (no net) -> +3V3_AUX
- C_RTL_4 pad 2: (no net) -> GND
- C_RTL_5 pad 1: (no net) -> +3V3_AUX
- C_RTL_5 pad 2: (no net) -> GND
- C_RTL_6 pad 1: (no net) -> +3V3_AUX
- C_RTL_6 pad 2: (no net) -> GND
- C_RTL_BULK pad 1: (no net) -> +3V3_AUX
- C_RTL_BULK pad 2: (no net) -> GND
- C_VB_J10 pad 1: (no net) -> VBUS_J10
- C_VB_J10 pad 2: (no net) -> GND
- C_VB_J11 pad 1: (no net) -> VBUS_J11
- C_VB_J11 pad 2: (no net) -> GND
- C_VB_J8 pad 1: (no net) -> VBUS_J8
- C_VB_J8 pad 2: (no net) -> GND
- C_VB_J9 pad 1: (no net) -> VBUS_J9
- C_VB_J9 pad 2: (no net) -> GND
- C_VIN_BULK pad 1: (no net) -> VIN_12V
- C_VIN_BULK pad 2: (no net) -> GND
- C_VIN_HF pad 1: (no net) -> VIN_12V
- C_VIN_HF pad 2: (no net) -> GND
- D1 pad 1: (no net) -> +3V3_AUX
- D1 pad 2: (no net) -> N$22
- D2 pad 1: (no net) -> CM5_GPIO_STATUS
- D2 pad 2: (no net) -> N$23
- D3 pad 1: (no net) -> ETH0_LED_ACT
- D3 pad 2: (no net) -> N$24
- D4 pad 1: (no net) -> ETH1_LED_ACT
- D4 pad 2: (no net) -> N$25
- D5 pad 1: (no net) -> NVME_ACT_N
- D5 pad 2: (no net) -> N$26
- D6 pad 1: (no net) -> VBUS_USB1
- D6 pad 2: (no net) -> GND1
- D_BAT pad 1: (no net) -> N$21
- D_BAT pad 2: (no net) -> V_BAT
- D_HDMI_CTL_1 pad 1: (no net) -> HDMI_CEC
- D_HDMI_CTL_1 pad 2: (no net) -> GND
- D_HDMI_CTL_2 pad 1: (no net) -> HDMI_HPD
- D_HDMI_CTL_2 pad 2: (no net) -> GND
- D_POE_1 pad 1: (no net) -> ETH0_CT_A
- D_POE_1 pad 2: (no net) -> POE_VIN_POS
- D_POE_2 pad 1: (no net) -> ETH0_CT_B
- D_POE_2 pad 2: (no net) -> POE_VIN_POS
- D_POE_3 pad 1: (no net) -> PoE_GND
- D_POE_3 pad 2: (no net) -> ETH0_CT_A
- D_POE_4 pad 1: (no net) -> PoE_GND
- D_POE_4 pad 2: (no net) -> ETH0_CT_B
- D_POE_OR pad 1: (no net) -> PoE_SEC_RECT2
- D_POE_OR pad 2: (no net) -> VIN_12V
- D_POE_SEC pad 1: (no net) -> PoE_SEC_HI1
- D_POE_SEC pad 2: (no net) -> PoE_SEC_RECT
- D_POE_TVS pad 1: (no net) -> POE_VIN_POS
- D_POE_TVS pad 2: (no net) -> PoE_GND
- D_TVS_J10 pad 1: (no net) -> VBUS_J10
- D_TVS_J10 pad 2: (no net) -> GND
- D_TVS_J11 pad 1: (no net) -> VBUS_J11
- D_TVS_J11 pad 2: (no net) -> GND
- D_TVS_J8 pad 1: (no net) -> VBUS_J8
- D_TVS_J8 pad 2: (no net) -> GND
- D_TVS_J9 pad 1: (no net) -> VBUS_J9
- D_TVS_J9 pad 2: (no net) -> GND
- FB_AVDD_1 pad 1: (no net) -> +3V3_AUX
- FB_AVDD_1 pad 2: (no net) -> AVDD_HDMI
- FB_AVDD_2 pad 1: (no net) -> +3V3_AUX
- FB_AVDD_2 pad 2: (no net) -> AVDD_PCIE
- FB_AVDD_3 pad 1: (no net) -> +3V3_AUX
- FB_AVDD_3 pad 2: (no net) -> AVDD_ETH0
- FB_AVDD_4 pad 1: (no net) -> +3V3_AUX
- FB_AVDD_4 pad 2: (no net) -> AVDD_ETH1
- FB_HDMI_5V pad 1: (no net) -> +5V
- FB_HDMI_5V pad 2: (no net) -> HDMI_5V_OUT1
- J10 pad 1: (no net) -> VBUS_J10
- J10 pad 10: (no net) -> GND
- J10 pad 2: (no net) -> HUB_P3_DM
- J10 pad 3: (no net) -> HUB_P3_DP
- J10 pad 4: (no net) -> GND
- J10 pad 5: (no net) -> HUB_P3_TX_N
- J10 pad 6: (no net) -> HUB_P3_TX_P
- J10 pad 8: (no net) -> HUB_P3_RX_N
- J10 pad 9: (no net) -> HUB_P3_RX_P
- J11 pad 1: (no net) -> VBUS_J11
- J11 pad 10: (no net) -> GND
- J11 pad 2: (no net) -> HUB_P4_DM
- J11 pad 3: (no net) -> HUB_P4_DP
- J11 pad 4: (no net) -> GND
- J11 pad 5: (no net) -> HUB_P4_TX_N
- J11 pad 6: (no net) -> HUB_P4_TX_P
- J11 pad 8: (no net) -> HUB_P4_RX_N
- J11 pad 9: (no net) -> HUB_P4_RX_P
- J12 pad 1: (no net) -> HDMI_TX2_P
- J12 pad 10: (no net) -> HDMI_CLK_P
- J12 pad 11: (no net) -> GND
- J12 pad 12: (no net) -> HDMI_CLK_N
- J12 pad 13: (no net) -> HDMI_CEC
- J12 pad 15: (no net) -> HDMI_DDC_SCL
- J12 pad 16: (no net) -> HDMI_DDC_SDA
- J12 pad 17: (no net) -> GND
- J12 pad 18: (no net) -> HDMI_5V_OUT
- J12 pad 19: (no net) -> HDMI_HPD
- J12 pad 2: (no net) -> GND
- J12 pad 3: (no net) -> HDMI_TX2_N
- J12 pad 4: (no net) -> HDMI_TX1_P
- J12 pad 5: (no net) -> GND
- J12 pad 6: (no net) -> HDMI_TX1_N
- J12 pad 7: (no net) -> HDMI_TX0_P
- J12 pad 8: (no net) -> GND
- J12 pad 9: (no net) -> HDMI_TX0_N
- J12 pad SH: (no net) -> GND
- J13 pad 1: (no net) -> +3V3_AUX
- J13 pad 14: (no net) -> GND
- J13 pad 17: (no net) -> +3V3_AUX
- J13 pad 2: (no net) -> +5V
- J13 pad 20: (no net) -> GND
- J13 pad 25: (no net) -> GND
- J13 pad 30: (no net) -> GND
- J13 pad 34: (no net) -> GND
- J13 pad 39: (no net) -> GND
- J13 pad 4: (no net) -> +5V
- J13 pad 6: (no net) -> GND
- J13 pad 9: (no net) -> GND
- J15 pad 1: (no net) -> GND
- J15 pad 2: (no net) -> +5V
- J15 pad 3: (no net) -> FAN_TACH
- J15 pad 4: (no net) -> FAN_PWM
- J3 pad 1: (no net) -> ETH0_MDI0_P
- J3 pad 2: (no net) -> ETH0_MDI0_N
- J3 pad 3: (no net) -> ETH0_MDI1_P
- J3 pad 4: (no net) -> ETH0_MDI2_P
- J3 pad 5: (no net) -> ETH0_MDI2_N
- J3 pad 6: (no net) -> ETH0_MDI1_N
- J3 pad 7: (no net) -> ETH0_MDI3_P
- J3 pad 8: (no net) -> ETH0_MDI3_N
- J4 pad 1: (no net) -> ETH1_MDI0_P
- J4 pad 2: (no net) -> ETH1_MDI0_N
- J4 pad 3: (no net) -> ETH1_MDI1_P
- J4 pad 4: (no net) -> ETH1_MDI2_P
- J4 pad 5: (no net) -> ETH1_MDI2_N
- J4 pad 6: (no net) -> ETH1_MDI1_N
- J4 pad 7: (no net) -> ETH1_MDI3_P
- J4 pad 8: (no net) -> ETH1_MDI3_N
- J5 pad 1: (no net) -> __NC__1
- J5 pad 10: (no net) -> __NC__1
- J5 pad 11: (no net) -> NVME_ACT_N
- J5 pad 12: (no net) -> __NC__1
- J5 pad 13: (no net) -> __NC__1
- J5 pad 14: (no net) -> __NC__1
- J5 pad 15: (no net) -> __NC__1
- J5 pad 16: (no net) -> __NC__1
- J5 pad 17: (no net) -> __NC__1
- J5 pad 18: (no net) -> __NC__1
- J5 pad 19: (no net) -> __NC__1
- J5 pad 2: (no net) -> __NC__1
- J5 pad 20: (no net) -> __NC__1
- J5 pad 21: (no net) -> __NC__1
- J5 pad 22: (no net) -> __NC__1
- J5 pad 23: (no net) -> __NC__1
- J5 pad 24: (no net) -> __NC__1
- J5 pad 25: (no net) -> PCIE0_REFCLK_N
- J5 pad 26: (no net) -> __NC__1
- J5 pad 27: (no net) -> PCIE0_REFCLK_P
- J5 pad 28: (no net) -> __NC__1
- J5 pad 29: (no net) -> PCIE0_RX_P
- J5 pad 3: (no net) -> __NC__1
- J5 pad 30: (no net) -> __NC__1
- J5 pad 31: (no net) -> PCIE0_RX_N
- J5 pad 32: (no net) -> __NC__1
- J5 pad 33: (no net) -> PCIE0_TX_N
- J5 pad 34: (no net) -> __NC__1
- J5 pad 35: (no net) -> PCIE0_TX_P
- J5 pad 36: (no net) -> __NC__1
- J5 pad 37: (no net) -> __NC__1
- J5 pad 38: (no net) -> __NC__1
- J5 pad 39: (no net) -> __NC__1
- J5 pad 4: (no net) -> __NC__1
- J5 pad 40: (no net) -> __NC__1
- J5 pad 41: (no net) -> __NC__1
- J5 pad 42: (no net) -> __NC__1
- J5 pad 43: (no net) -> __NC__1
- J5 pad 44: (no net) -> __NC__1
- J5 pad 45: (no net) -> __NC__1
- J5 pad 46: (no net) -> __NC__1
- J5 pad 47: (no net) -> __NC__1
- J5 pad 48: (no net) -> __NC__1
- J5 pad 49: (no net) -> __NC__1
- J5 pad 5: (no net) -> __NC__1
- J5 pad 50: (no net) -> PCIE0_PERST_N
- J5 pad 51: (no net) -> __NC__1
- J5 pad 52: (no net) -> PCIE0_CLKREQ_N
- J5 pad 53: (no net) -> __NC__1
- J5 pad 54: (no net) -> PCIE0_WAKE_N
- J5 pad 55: (no net) -> __NC__1
- J5 pad 56: (no net) -> __NC__1
- J5 pad 57: (no net) -> __NC__1
- J5 pad 58: (no net) -> __NC__1
- J5 pad 59: (no net) -> __NC__1
- J5 pad 6: (no net) -> __NC__1
- J5 pad 60: (no net) -> __NC__1
- J5 pad 61: (no net) -> __NC__1
- J5 pad 62: (no net) -> __NC__1
- J5 pad 63: (no net) -> __NC__1
- J5 pad 64: (no net) -> __NC__1
- J5 pad 65: (no net) -> __NC__1
- J5 pad 66: (no net) -> __NC__1
- J5 pad 67: (no net) -> __NC__1
- J5 pad 68: (no net) -> __NC__1
- J5 pad 69: (no net) -> +3V3_AUX
- J5 pad 7: (no net) -> __NC__1
- J5 pad 70: (no net) -> GND
- J5 pad 71: (no net) -> +3V3_AUX
- J5 pad 72: (no net) -> GND
- J5 pad 73: (no net) -> +3V3_AUX
- J5 pad 74: (no net) -> GND
- J5 pad 75: (no net) -> +3V3_AUX
- J5 pad 8: (no net) -> __NC__1
- J5 pad 9: (no net) -> __NC__1
- J6 pad 1: (no net) -> GND
- J6 pad 10: (no net) -> __NC__1
- J6 pad 11: (no net) -> GND
- J6 pad 12: (no net) -> __NC__1
- J6 pad 13: (no net) -> __NC__1
- J6 pad 14: (no net) -> __NC__1
- J6 pad 15: (no net) -> GND
- J6 pad 16: (no net) -> __NC__1
- J6 pad 17: (no net) -> GND
- J6 pad 18: (no net) -> __NC__1
- J6 pad 19: (no net) -> GND
- J6 pad 2: (no net) -> +3V3_AUX
- J6 pad 20: (no net) -> __NC__1
- J6 pad 21: (no net) -> E_PCIE_TX_P
- J6 pad 22: (no net) -> __NC__1
- J6 pad 23: (no net) -> E_PCIE_TX_N
- J6 pad 24: (no net) -> __NC__1
- J6 pad 25: (no net) -> GND
- J6 pad 26: (no net) -> __NC__1
- J6 pad 27: (no net) -> __NC__1
- J6 pad 28: (no net) -> __NC__1
- J6 pad 29: (no net) -> E_PCIE_RX_P
- J6 pad 3: (no net) -> __NC__1
- J6 pad 30: (no net) -> __NC__1
- J6 pad 31: (no net) -> E_PCIE_RX_N
- J6 pad 32: (no net) -> __NC__1
- J6 pad 33: (no net) -> GND
- J6 pad 34: (no net) -> __NC__1
- J6 pad 35: (no net) -> __NC__1
- J6 pad 36: (no net) -> USB2_1_DP
- J6 pad 37: (no net) -> __NC__1
- J6 pad 38: (no net) -> USB2_1_DM
- J6 pad 39: (no net) -> GND
- J6 pad 4: (no net) -> +3V3_AUX
- J6 pad 40: (no net) -> __NC__1
- J6 pad 41: (no net) -> E_PCIE_REFCLK_P
- J6 pad 42: (no net) -> __NC__1
- J6 pad 43: (no net) -> E_PCIE_REFCLK_N
- J6 pad 44: (no net) -> __NC__1
- J6 pad 45: (no net) -> GND
- J6 pad 46: (no net) -> WIFI_DISABLE1_N
- J6 pad 47: (no net) -> __NC__1
- J6 pad 48: (no net) -> WIFI_DISABLE2_N
- J6 pad 49: (no net) -> __NC__1
- J6 pad 5: (no net) -> __NC__1
- J6 pad 50: (no net) -> PCIE1_CLKREQ_N
- J6 pad 51: (no net) -> GND
- J6 pad 52: (no net) -> __NC__1
- J6 pad 53: (no net) -> __NC__1
- J6 pad 54: (no net) -> __NC__1
- J6 pad 55: (no net) -> __NC__1
- J6 pad 56: (no net) -> PCIE1_PERST_N
- J6 pad 57: (no net) -> GND
- J6 pad 58: (no net) -> __NC__1
- J6 pad 59: (no net) -> __NC__1
- J6 pad 6: (no net) -> __NC__1
- J6 pad 60: (no net) -> __NC__1
- J6 pad 61: (no net) -> __NC__1
- J6 pad 62: (no net) -> __NC__1
- J6 pad 63: (no net) -> GND
- J6 pad 64: (no net) -> __NC__1
- J6 pad 65: (no net) -> __NC__1
- J6 pad 66: (no net) -> __NC__1
- J6 pad 67: (no net) -> __NC__1
- J6 pad 68: (no net) -> __NC__1
- J6 pad 69: (no net) -> GND
- J6 pad 7: (no net) -> GND
- J6 pad 70: (no net) -> __NC__1
- J6 pad 71: (no net) -> __NC__1
- J6 pad 72: (no net) -> +3V3_AUX
- J6 pad 73: (no net) -> __NC__1
- J6 pad 74: (no net) -> +3V3_AUX
- J6 pad 75: (no net) -> GND
- J6 pad 8: (no net) -> __NC__1
- J6 pad 9: (no net) -> GND
- J7 pad A1: (no net) -> GND1
- J7 pad A12: (no net) -> GND1
- J7 pad A4: (no net) -> VBUS_USB1
- J7 pad A5: (no net) -> USB_CC1
- J7 pad A6: (no net) -> USB_DP1
- J7 pad A7: (no net) -> USB_DM1
- J7 pad A8: (no net) -> USB_SBU1
- J7 pad A9: (no net) -> VBUS_USB1
- J7 pad B1: (no net) -> GND1
- J7 pad B12: (no net) -> GND1
- J7 pad B4: (no net) -> VBUS_USB1
- J7 pad B5: (no net) -> USB_CC2
- J7 pad B6: (no net) -> USB_DP1
- J7 pad B7: (no net) -> USB_DM1
- J7 pad B8: (no net) -> USB_SBU2
- J7 pad B9: (no net) -> VBUS_USB1
- J7 pad S1: (no net) -> GND1
- J8 pad 1: (no net) -> VBUS_J8
- J8 pad 10: (no net) -> GND
- J8 pad 2: (no net) -> HUB_P1_DM
- J8 pad 3: (no net) -> HUB_P1_DP
- J8 pad 4: (no net) -> GND
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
